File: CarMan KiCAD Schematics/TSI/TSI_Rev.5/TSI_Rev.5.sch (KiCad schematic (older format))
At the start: 26 parts, among them J1 J1, J10 J10, J11 J11, J12 J12, J13.1 Conn_01x06, J13.2 Conn_01x06, J14 J14, J15 J15, J16 J16, J17 J17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

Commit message: TSI Footprinting (100%) - Created symbol for connector J1
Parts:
- J1: footprint (none) -> TSI_Rev_2021_Footprint_Lib:Molex-0010844030; Note (none) -> This is custom, could not find on internet
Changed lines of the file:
@@
 F 0 "J1" H 900 950 50  0000 L CNN
 F 1 "J1" H 900 950 50  0001 L CNN
-F 2 "" H 950 750 50  0001 C CNN
+F 2 "TSI_Rev_2021_Footprint_Lib:Molex-0010844030" H 950 750 50  0001 C CNN
 F 3 "https://www.molex.com/pdm_docs/sd/010844020_sd.pdf" H 950 750 50  0001 C CNN
+F 4 "This is custom, could not find on internet" H 950 750 50  0001 C CNN "Note"
 	1    950  750
 	1    0    0    -1

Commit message: Started TSI PCB
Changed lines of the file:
@@
 F1 "PCDC_Circuit.sch" 79
 F2 "Throttle_HV" I R 3100 6400 50
-F3 "MC+" I L 1550 6000 50
+F3 "MC_Voltage" I L 1550 6000 50
 F4 "HV-" I L 1550 5900 50
 F5 "HV+" I L 1550 5800 50
-F6 "TSV_V" I L 1550 6100 50
+F6 "TSV_Voltage" I L 1550 6100 50
 F7 "IO_Ground" I R 3100 6500 50
 F8 "1.24VREF" I R 3100 6200 50
@@
 Brake_Pressed_HV
 Text Label 700  6000 0    50   ~ 0
-MC+
+MC_Voltage
 Wire Wire Line
 	1550 2800 2050 2800
@@
 	6200 6650 6800 6650
 $Sheet
-S 4800 6200 1400 1350
+S 4800 6200 1400 1400
 U 5F98EBE9
 F0 "Sensors_Throttle_Voltage" 50
@@
 F10 "Throttle_HV" I L 4800 7200 50
 F11 "TSV_Voltage" I L 4800 6900 50
-F12 "MC_Voltage" I L 4800 6800 50
+F12 "MC+" I L 4800 6800 50
 F13 "HV+" I L 4800 7000 50
 F14 "HV-" I L 4800 7100 50
 F15 "A1_HV" I L 4800 7300 50
 F16 "A2_HV" I L 4800 7400 50
+F17 "MC_Voltage" I L 4800 7500 50
 $EndSheet
 Text Notes 5650 6350 0    47   ~ 0
@@
 Text Notes 9650 3950 2    50   ~ 0
 LV\n
+Text Label 4200 7500 0    50   ~ 0
+MC_Voltage
+Wire Wire Line
+	4200 7500 4800 7500
 $EndSCHEMATC

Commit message: - Updated logic header footprints on TSI
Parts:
- J13.1, J13.2: footprint TSI_Rev_2021_Footprint_Lib:Molex_MiniFit-JR-5556-06A_2x03x4.20mm_Straight -> Connector_PinSocket_2.54mm:PinSocket_1x06_P2.54mm_Vertical
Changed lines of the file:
@@
 F 0 "J13.2" H 5950 2100 50  0000 L CNN
 F 1 "Conn_01x06" H 6180 1701 50  0001 L CNN
-F 2 "TSI_Rev_2021_Footprint_Lib:Molex_MiniFit-JR-5556-06A_2x03x4.20mm_Straight" H 6100 1800 50  0001 C CNN
+F 2 "Connector_PinSocket_2.54mm:PinSocket_1x06_P2.54mm_Vertical" H 6100 1800 50  0001 C CNN
 F 3 "~" H 6100 1800 50  0001 C CNN
 	1    6100 1800
@@
 F 0 "J13.1" H 5700 2100 50  0000 L CNN
 F 1 "Conn_01x06" H 5930 1701 50  0001 L CNN
-F 2 "TSI_Rev_2021_Footprint_Lib:Molex_MiniFit-JR-5556-06A_2x03x4.20mm_Straight" H 5850 1800 50  0001 C CNN
+F 2 "Connector_PinSocket_2.54mm:PinSocket_1x06_P2.54mm_Vertical" H 5850 1800 50  0001 C CNN
 F 3 "~" H 5850 1800 50  0001 C CNN
 	1    5850 1800

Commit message: Started TSI layout
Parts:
- J1: symbol Connector_Generic:Conn_01x04 -> Connector_Generic:Conn_01x03
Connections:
- no-connect marks 10 -> 9
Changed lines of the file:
@@
 Text Label 700  7300 0    50   ~ 0
 AIRS+
-NoConn ~ 750  950
-$Comp
-L Connector_Generic:Conn_01x04 J1
+$Comp
+L Connector_Generic:Conn_01x03 J1
 U 1 1 5FC3F568
 P 950 750
@@
 Text Label 11100 3500 2    50   ~ 0
 Drive_BTN
-$Comp
-L TSI_Rev.5-rescue:Current_Sensor-CarMan_KiCAD_Library-TSI_Rev.5-rescue J?
-U 1 1 5FA558BE
-P 950 1300
-AR Path="/5F98EBE9/5FA558BE" Ref="J?"  Part="1"
-AR Path="/5FA558BE" Ref="J2"  Part="1"
-F 0 "J2" H 950 1300 50  0000 C CNN
-F 1 "Current_Sensor" H 950 500 50  0000 C CNN
-F 2 "TSI_Rev_2021_Footprint_Lib:Current Sensor" H 950 1300 50  0001 C CNN
-F 3 "" H 950 1300 50  0001 C CNN
-	1    950  1300
-	1    0    0    -1
-$EndComp
 NoConn ~ 1350 1950
 NoConn ~ 1350 1450
@@
 Wire Wire Line
 	4200 7500 4800 7500
+$Comp
+L TSI_Rev.5-rescue:Current_Sensor-CarMan_KiCAD_Library-TSI_Rev.5-rescue J?
+U 1 1 5FA558BE
+P 950 1300
+AR Path="/5F98EBE9/5FA558BE" Ref="J?"  Part="1"
+AR Path="/5FA558BE" Ref="J2"  Part="1"
+F 0 "J2" H 950 1300 50  0000 C CNN
+F 1 "Current_Sensor" H 950 500 50  0000 C CNN
+F 2 "TSI_Rev_2021_Footprint_Lib:Current Sensor" H 950 1300 50  0001 C CNN
+F 3 "" H 950 1300 50  0001 C CNN
+	1    950  1300
+	1    0    0    -1
+$EndComp
 $EndSCHEMATC

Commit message: Organizational Added jumper between chassis ground and can shield
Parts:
- added JP3: Jumper, Connector_PinHeader_2.54mm:PinHeader_1x02_P2.54mm_Vertical, symbol Device:Jumper
- J19: footprint TSI_Rev_2021_Footprint_Lib:Molex_MiniFit-JR-5556-06A_2x03x4.20mm_Straight -> Connector_PinSocket_2.54mm:PinSocket_1x08_P2.54mm_Vertical; symbol Connector_Generic:Conn_01x06 -> Connector_Generic:Conn_01x08
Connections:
- net CAN_Shield: now also JP3.1; no longer J6.4 (Pin_4)
- new net Chassis_GND: J6.4 (Pin_4), JP3.2
- no-connect marks 9 -> 11
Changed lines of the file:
@@
 Text Label 4950 2100 0    50   ~ 0
 Throttle_SEL
-Text Label 5150 3450 0    50   ~ 0
+Text Label 5150 3600 0    50   ~ 0
 Flowrate_5V
-Text Label 6700 3450 2    50   ~ 0
+Text Label 6700 3600 2    50   ~ 0
 5V
-Text Label 5150 3550 0    50   ~ 0
+Text Label 5150 3700 0    50   ~ 0
 Flowrate_RTN
-Text Label 6700 3550 2    50   ~ 0
+Text Label 6700 3700 2    50   ~ 0
 GLV_RTN
 Text Label 7300 800  2    50   ~ 0
@@
 Text Label 7450 850  0    50   ~ 0
 CAN_Shield
-Text Label 7450 950  0    50   ~ 0
-Chassis_GND
 Text Label 7450 750  0    50   ~ 0
 BP_CAN-
@@
 Wire Notes Line
 	6550 2600 6550 3100
-Text Label 6700 3650 2    50   ~ 0
+Text Label 6700 3800 2    50   ~ 0
 GLV_RTN
-Text Label 5150 3650 0    50   ~ 0
+Text Label 5150 3800 0    50   ~ 0
 FAULT_LED_RTN
 Wire Notes Line
@@
 Text Label 2000 2250 0    50   ~ 0
 Safety_Loop
-Text Label 6700 3350 2    49   ~ 0
+Text Label 6700 3500 2    49   ~ 0
 MRESET_Contact
-Text Label 5150 3350 0    49   ~ 0
+Text Label 5150 3500 0    49   ~ 0
 GEN_Fault_LED
 Text Label 4950 1800 0    49   ~ 0
@@
 Text Label 700  4950 0    50   ~ 0
 Flowrate
-Text Label 6700 3250 2    50   ~ 0
+Text Label 6700 3400 2    50   ~ 0
 Brake_Light
-Text Label 5150 3250 0    50   ~ 0
+Text Label 5150 3400 0    50   ~ 0
 Brake_Pressed
-Text Label 5150 3750 0    50   ~ 0
+Text Label 5150 3900 0    50   ~ 0
 Brake_Light_RTN
-Text Label 6700 3750 2    50   ~ 0
+Text Label 6700 3900 2    50   ~ 0
 GLV_RTN
 Text Label 11100 3600 2    50   ~ 0
@@
 Text Label 8100 5900 0    50   ~ 0
 COOL_24V
-Text Notes 7750 1250 0    50   ~ 0
-Battery Pack\nto TSI\n\n
 $Comp
 L Connector_Generic:Conn_01x04 J6
@@
 	5300 750  5600 750
 Wire Wire Line
-	5150 3250 6700 3250
-Wire Wire Line
-	5150 3350 6700 3350
-Wire Wire Line
-	5150 3450 6700 3450
-Wire Wire Line
-	5150 3550 6700 3550
-Wire Wire Line
-	5150 3650 6700 3650
-Wire Wire Line
-	5150 3750 6700 3750
-Wire Wire Line
-	5150 3850 6700 3850
-Text Label 5150 3850 0    50   ~ 0
+	5150 3400 6700 3400
+Wire Wire Line
+	5150 3500 6700 3500
+Wire Wire Line
+	5150 3600 6700 3600
+Wire Wire Line
+	5150 3700 6700 3700
+Wire Wire Line
+	5150 3800 6700 3800
+Wire Wire Line
+	5150 3900 6700 3900
+Wire Wire Line
+	5150 4000 6700 4000
+Text Label 5150 4000 0    50   ~ 0
 SCL_uC
-Text Label 6700 3850 2    50   ~ 0
+Text Label 6700 4000 2    50   ~ 0
 SCL_TSI
-Text Label 6200 3850 0    50   ~ 0
+Text Label 6200 4000 0    50   ~ 0
 SCL
 Wire Wire Line
-	5150 3950 6700 3950
-Text Label 5150 3950 0    50   ~ 0
+	5150 4100 6700 4100
+Text Label 5150 4100 0    50   ~ 0
 SDA_uC
-Text Label 6200 3950 0    50   ~ 0
+Text Label 6200 4100 0    50   ~ 0
 SDA
-Text Label 6700 3950 2    50   ~ 0
+Text Label 6700 4100 2    50   ~ 0
 SDA_TSI
 Text Label 700  6200 0    50   ~ 0
@@
 Text Label 1550 3100 0    50   ~ 0
 IMD_Status
-Text Notes 1600 3450 0    50   ~ 0
+Text Notes 1650 3650 0    50   ~ 0
 Testing Connector\n\n
 $Comp
-L Connector_Generic:Conn_01x06 J19
+L Connector_Generic:Conn_01x08 J19
 U 1 1 5FE0EFE1
-P 2250 2900
-F 0 "J19" H 2200 3200 50  0000 L CNN
-F 1 "J19" H 2200 3200 50  0001 L CNN
-F 2 "TSI_Rev_2021_Footprint_Lib:Molex_MiniFit-JR-5556-06A_2x03x4.20mm_Straight" H 2250 2900 50  0001 C CNN
-F 3 "~" H 2250 2900 50  0001 C CNN
-	1    2250 2900
+P 2250 3000
+F 0 "J19" H 2200 3400 50  0000 L CNN
+F 1 "J19" H 2200 3300 50  0001 L CNN
+F 2 "Connector_PinSocket_2.54mm:PinSocket_1x08_P2.54mm_Vertical" H 2250 3000 50  0001 C CNN
+F 3 "~" H 2250 3000 50  0001 C CNN
+	1    2250 3000
 	1    0    0    -1
 $EndComp
@@
 5V
 Wire Wire Line
-	5150 4050 6700 4050
-Text Label 5150 4050 0    50   ~ 0
+	5150 4200 6700 4200
+Text Label 5150 4200 0    50   ~ 0
 TSAL_RTN
-Text Label 6700 4050 2    50   ~ 0
+Text Label 6700 4200 2    50   ~ 0
 GLV_RTN
 $Comp
@@
 $EndComp
 Wire Wire Line
-	5150 4150 6700 4150
-Text Label 5150 4150 0    50   ~ 0
+	5150 4300 6700 4300
+Text Label 5150 4300 0    50   ~ 0
 AIRS-
-Text Label 6700 4150 2    50   ~ 0
+Text Label 6700 4300 2    50   ~ 0
 GLV_RTN
 $Comp
@@
 Wire Wire Line
 	5950 4850 6450 4850
-Wire Wire Line
-	7450 850  7450 950
-Connection ~ 7450 950
 $Comp
 L power:PWR_FLAG #FLG0101
@@
 Text Label 10400 750  0    49   ~ 0
 GLV_RTN
-Text Label 10400 850  0    50   ~ 0
-SL1_In
 $Sheet
 S 8850 2950 1500 1450
@@
 	1    0    0    -1
 $EndComp
+NoConn ~ 2050 3300
+NoConn ~ 2050 3400
+$Comp
+L Device:Jumper JP?
+U 1 1 601967AD
+P 5900 3300
+AR Path="/6196BF15/601967AD" Ref="JP?"  Part="1"
+AR Path="/601967AD" Ref="JP3"  Part="1"
+F 0 "JP3" H 6100 3400 50  0000 R CNN
+F 1 "Jumper" H 6600 3300 50  0001 R CNN
+F 2 "Connector_PinHeader_2.54mm:PinHeader_1x02_P2.54mm_Vertical" H 5900 3300 50  0001 C CNN
+F 3 "~" H 5900 3300 50  0001 C CNN
+	1    5900 3300
+	1    0    0    -1
+$EndComp
+Text Label 5150 3300 0    50   ~ 0
+CAN_Shield
+Text Label 6700 3300 2    50   ~ 0
+Chassis_GND
+Wire Wire Line
+	6700 3300 6200 3300
+Wire Wire Line
+	5150 3300 5600 3300
+Text Notes 7550 1250 0    50   ~ 0
+Battery Pack\nto TSI\n\n
+Text Label 7450 950  0    50   ~ 0
+Chassis_GND
+Text Label 10400 850  0    50   ~ 0
+SL1_In
 $EndSCHEMATC

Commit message: TSI (~97%)
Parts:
- added J21: J21, Connector_PinSocket_2.54mm:PinSocket_1x04_P2.54mm_Vertical, symbol Connector_Generic:Conn_01x04
- added J23: J23, Connector_PinSocket_2.54mm:PinSocket_1x02_P2.54mm_Vertical, symbol Connector_Generic:Conn_01x02
- J19: footprint Connector_PinSocket_2.54mm:PinSocket_1x08_P2.54mm_Vertical -> Connector_PinSocket_2.54mm:PinSocket_1x04_P2.54mm_Vertical; symbol Connector_Generic:Conn_01x08 -> Connector_Generic:Conn_01x04
- J22: renamed from J21; value J21 -> J22
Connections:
- net IMD_Status: now also J19.3 (Pin_3); no longer J19.5 (Pin_5)
- net PC_Ready: now also J19.1 (Pin_1); no longer J19.3 (Pin_3)
- net SCL: now also J23.2 (Pin_2); no longer J19.2 (Pin_2)
- net SDA: now also J23.1 (Pin_1); no longer J19.1 (Pin_1)
- net SL1_In: now also J19.2 (Pin_2); no longer J19.4 (Pin_4)
- net Throttle_SEL: now also J19.4 (Pin_4); no longer J19.6 (Pin_6)
- no-connect marks 11 -> 13
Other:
- note added: "Left Side\nTesting Connector\n\n"
- note added: "Right Side\nTesting Connector\n\n"
- note removed: "Testing Connector\n\n"
- moved on the sheet: J22
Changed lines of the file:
@@
 Text Label 2000 1750 0    50   ~ 0
 AMS_FAULT_LED
+Text Label 4400 2800 0    50   ~ 0
+SCL
 Text Label 1550 2800 0    50   ~ 0
-SCL
-Text Label 1550 3000 0    50   ~ 0
 SL1_In
-Text Label 1550 2700 0    50   ~ 0
+Text Label 4400 2700 0    50   ~ 0
 SDA
 Text Label 550  2700 0    50   ~ 0
@@
 	10400 950  10850 950
 Wire Wire Line
-	1550 2700 2050 2700
-Wire Wire Line
 	2000 1750 2600 1750
 Text Label 11100 4800 2    50   ~ 0
@@
 Text Label 11100 6100 2    50   ~ 0
 IMD_FAULT_LED
-Text Notes 2550 3250 0    50   ~ 0
+Text Notes 3300 3250 0    50   ~ 0
 LSP IMD & AMS Reset \nButton\n
-Text Label 2550 2700 0    50   ~ 0
+Text Label 3300 2700 0    50   ~ 0
 IMD_Status
-Text Label 2550 2800 0    50   ~ 0
+Text Label 3300 2800 0    50   ~ 0
 IMD_Button_RTN
 Wire Wire Line
-	2550 2800 3200 2800
-Wire Wire Line
-	2550 2700 3200 2700
+	3300 2800 3950 2800
+Wire Wire Line
+	3300 2700 3950 2700
 Text Label 11100 6000 2    50   ~ 0
 IMD_Button_RTN
@@
 MC_Voltage
 Wire Wire Line
+	1550 2700 2050 2700
+Wire Wire Line
+	1550 3000 2050 3000
+Wire Wire Line
+	1550 2900 2050 2900
+Wire Wire Line
 	1550 2800 2050 2800
-Wire Wire Line
-	1550 2900 2050 2900
-Wire Wire Line
-	1550 3200 2050 3200
-Wire Wire Line
-	1550 3100 2050 3100
-Wire Wire Line
-	1550 3000 2050 3000
+Text Label 1550 2700 0    50   ~ 0
+PC_Ready
+Text Label 1550 3000 0    50   ~ 0
+Throttle_SEL
 Text Label 1550 2900 0    50   ~ 0
-PC_Ready
-Text Label 1550 3200 0    50   ~ 0
-Throttle_SEL
-Text Label 1550 3100 0    50   ~ 0
 IMD_Status
-Text Notes 1650 3650 0    50   ~ 0
-Testing Connector\n\n
-$Comp
-L Connector_Generic:Conn_01x08 J19
+Text Notes 1600 3250 0    50   ~ 0
+Left Side\nTesting Connector\n\n
+$Comp
+L Connector_Generic:Conn_01x04 J19
 U 1 1 5FE0EFE1
-P 2250 3000
-F 0 "J19" H 2200 3400 50  0000 L CNN
-F 1 "J19" H 2200 3300 50  0001 L CNN
-F 2 "Connector_PinSocket_2.54mm:PinSocket_1x08_P2.54mm_Vertical" H 2250 3000 50  0001 C CNN
-F 3 "~" H 2250 3000 50  0001 C CNN
-	1    2250 3000
+P 2250 2800
+F 0 "J19" H 2200 3000 50  0000 L CNN
+F 1 "J19" H 2200 3100 50  0001 L CNN
+F 2 "Connector_PinSocket_2.54mm:PinSocket_1x04_P2.54mm_Vertical" H 2250 2800 50  0001 C CNN
+F 3 "~" H 2250 2800 50  0001 C CNN
+	1    2250 2800
 	1    0    0    -1
 $EndComp
@@
 $EndComp
 $Comp
-L Connector_Generic:Conn_01x04 J21
+L Connector_Generic:Conn_01x04 J22
 U 1 1 5FDCB93A
-P 3400 2800
-F 0 "J21" H 3350 3000 50  0000 L CNN
-F 1 "J21" H 3350 3000 50  0001 L CNN
-F 2 "TSI_Rev_2021_Footprint_Lib:Molex_MiniFit-JR-5556-04A_2x02x4.20mm_Straight" H 3400 2800 50  0001 C CNN
-F 3 "~" H 3400 2800 50  0001 C CNN
-	1    3400 2800
-	1    0    0    -1
-$EndComp
-Text Label 2550 2900 0    50   ~ 0
+P 4150 2800
+F 0 "J22" H 4100 3000 50  0000 L CNN
+F 1 "J22" H 4100 3000 50  0001 L CNN
+F 2 "TSI_Rev_2021_Footprint_Lib:Molex_MiniFit-JR-5556-04A_2x02x4.20mm_Straight" H 4150 2800 50  0001 C CNN
+F 3 "~" H 4150 2800 50  0001 C CNN
+	1    4150 2800
+	1    0    0    -1
+$EndComp
+Text Label 3300 2900 0    50   ~ 0
 AMS_Status
-Text Label 2550 3000 0    50   ~ 0
+Text Label 3300 3000 0    50   ~ 0
 AMS_Button_RTN
 Wire Wire Line
-	2550 3000 3200 3000
-Wire Wire Line
-	2550 2900 3200 2900
+	3300 3000 3950 3000
+Wire Wire Line
+	3300 2900 3950 2900
 Wire Wire Line
 	3600 950  2950 950
@@
 	1    0    0    -1
 $EndComp
-NoConn ~ 2050 3300
-NoConn ~ 2050 3400
 $Comp
 L Device:Jumper JP?
@@
 Text Label 10400 850  0    50   ~ 0
 SL1_In
+$Comp
+L Connector_Generic:Conn_01x02 J23
+U 1 1 600AD19A
+P 4800 2700
+F 0 "J23" H 4750 2800 50  0000 L CNN
+F 1 "J23" H 4750 2800 50  0001 L CNN
+F 2 "Connector_PinSocket_2.54mm:PinSocket_1x02_P2.54mm_Vertical" H 4800 2700 50  0001 C CNN
+F 3 "~" H 4800 2700 50  0001 C CNN
+	1    4800 2700
+	1    0    0    -1
+$EndComp
+Wire Wire Line
+	4600 2800 4400 2800
+Wire Wire Line
+	4600 2700 4400 2700
+Text Notes 2450 3250 0    50   ~ 0
+Right Side\nTesting Connector\n\n
+NoConn ~ 2800 2700
+NoConn ~ 2800 2800
+NoConn ~ 2800 2900
+$Comp
+L Connector_Generic:Conn_01x04 J21
+U 1 1 60224CCE
+P 3000 2800
+F 0 "J21" H 2950 3000 50  0000 L CNN
+F 1 "J21" H 2950 3100 50  0001 L CNN
+F 2 "Connector_PinSocket_2.54mm:PinSocket_1x04_P2.54mm_Vertical" H 3000 2800 50  0001 C CNN
+F 3 "~" H 3000 2800 50  0001 C CNN
+	1    3000 2800
+	1    0    0    -1
+$EndComp
+NoConn ~ 2800 3000
 $EndSCHEMATC

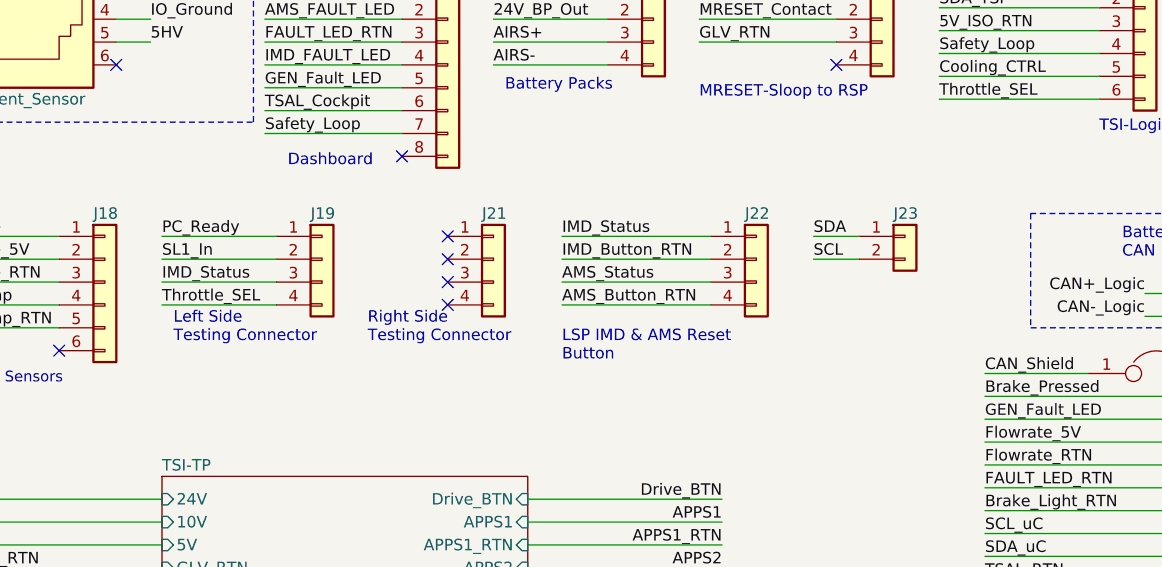
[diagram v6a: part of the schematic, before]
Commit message: TSI (~98%) - Added right side testing connector - Finish left side testing connector - Added Caps to HV side
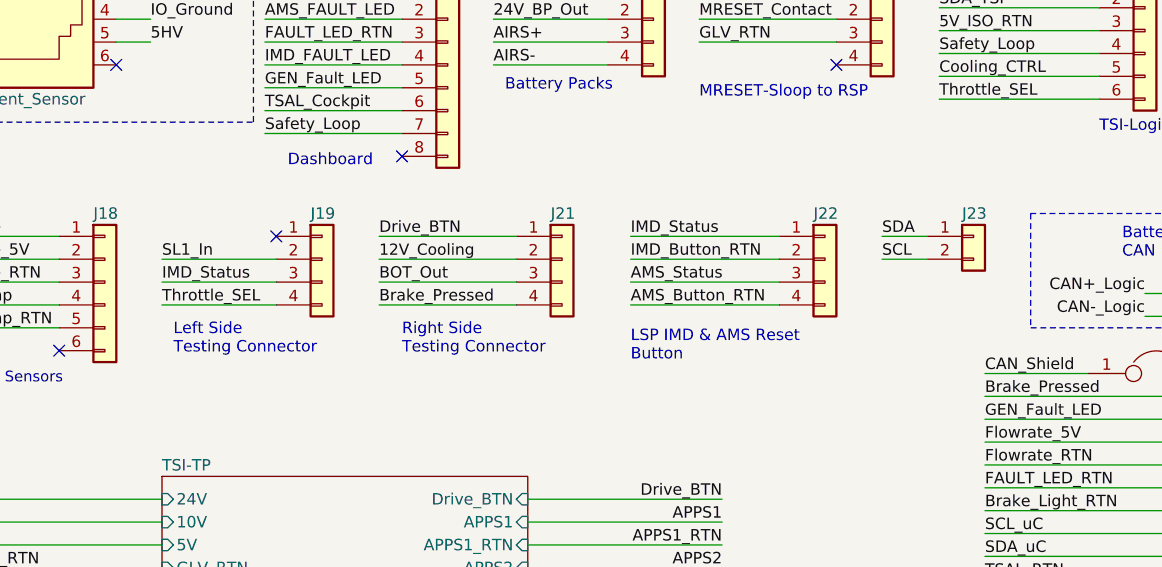
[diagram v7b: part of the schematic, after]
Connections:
- net 12V_Cooling: now also J21.2 (Pin_2)
- net BOT_Out: now also J21.3 (Pin_3)
- net Brake_Light: now also J21.4 (Pin_4)
- net Drive_BTN: now also J21.1 (Pin_1)
- net PC_Ready: no longer J19.1 (Pin_1)
- no-connect marks 13 -> 10
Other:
- moved on the sheet: J21, J22, J23
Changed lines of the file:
@@
 Text Label 2000 1750 0    50   ~ 0
 AMS_FAULT_LED
-Text Label 4400 2800 0    50   ~ 0
+Text Label 4700 2800 0    50   ~ 0
 SCL
 Text Label 1550 2800 0    50   ~ 0
 SL1_In
-Text Label 4400 2700 0    50   ~ 0
+Text Label 4700 2700 0    50   ~ 0
 SDA
 Text Label 550  2700 0    50   ~ 0
@@
 Text Label 6700 3400 2    50   ~ 0
 Brake_Light
-Text Label 5150 3400 0    50   ~ 0
-Brake_Pressed
 Text Label 5150 3900 0    50   ~ 0
 Brake_Light_RTN
@@
 Text Label 11100 6100 2    50   ~ 0
 IMD_FAULT_LED
-Text Notes 3300 3250 0    50   ~ 0
+Text Notes 3600 3250 0    50   ~ 0
 LSP IMD & AMS Reset \nButton\n
-Text Label 3300 2700 0    50   ~ 0
+Text Label 3600 2700 0    50   ~ 0
 IMD_Status
-Text Label 3300 2800 0    50   ~ 0
+Text Label 3600 2800 0    50   ~ 0
 IMD_Button_RTN
 Wire Wire Line
-	3300 2800 3950 2800
-Wire Wire Line
-	3300 2700 3950 2700
+	3600 2800 4250 2800
+Wire Wire Line
+	3600 2700 4250 2700
 Text Label 11100 6000 2    50   ~ 0
 IMD_Button_RTN
@@
 MC_Voltage
 Wire Wire Line
-	1550 2700 2050 2700
-Wire Wire Line
 	1550 3000 2050 3000
 Wire Wire Line
@@
 Wire Wire Line
 	1550 2800 2050 2800
-Text Label 1550 2700 0    50   ~ 0
-PC_Ready
 Text Label 1550 3000 0    50   ~ 0
 Throttle_SEL
 Text Label 1550 2900 0    50   ~ 0
 IMD_Status
-Text Notes 1600 3250 0    50   ~ 0
+Text Notes 1600 3300 0    50   ~ 0
 Left Side\nTesting Connector\n\n
 $Comp
@@
 L Connector_Generic:Conn_01x04 J22
 U 1 1 5FDCB93A
-P 4150 2800
-F 0 "J22" H 4100 3000 50  0000 L CNN
-F 1 "J22" H 4100 3000 50  0001 L CNN
-F 2 "TSI_Rev_2021_Footprint_Lib:Molex_MiniFit-JR-5556-04A_2x02x4.20mm_Straight" H 4150 2800 50  0001 C CNN
-F 3 "~" H 4150 2800 50  0001 C CNN
-	1    4150 2800
-	1    0    0    -1
-$EndComp
-Text Label 3300 2900 0    50   ~ 0
+P 4450 2800
+F 0 "J22" H 4400 3000 50  0000 L CNN
+F 1 "J22" H 4400 3000 50  0001 L CNN
+F 2 "TSI_Rev_2021_Footprint_Lib:Molex_MiniFit-JR-5556-04A_2x02x4.20mm_Straight" H 4450 2800 50  0001 C CNN
+F 3 "~" H 4450 2800 50  0001 C CNN
+	1    4450 2800
+	1    0    0    -1
+$EndComp
+Text Label 3600 2900 0    50   ~ 0
 AMS_Status
-Text Label 3300 3000 0    50   ~ 0
+Text Label 3600 3000 0    50   ~ 0
 AMS_Button_RTN
 Wire Wire Line
-	3300 3000 3950 3000
-Wire Wire Line
-	3300 2900 3950 2900
+	3600 3000 4250 3000
+Wire Wire Line
+	3600 2900 4250 2900
 Wire Wire Line
 	3600 950  2950 950
@@
 L Connector_Generic:Conn_01x02 J23
 U 1 1 600AD19A
-P 4800 2700
-F 0 "J23" H 4750 2800 50  0000 L CNN
-F 1 "J23" H 4750 2800 50  0001 L CNN
-F 2 "Connector_PinSocket_2.54mm:PinSocket_1x02_P2.54mm_Vertical" H 4800 2700 50  0001 C CNN
-F 3 "~" H 4800 2700 50  0001 C CNN
-	1    4800 2700
-	1    0    0    -1
-$EndComp
-Wire Wire Line
-	4600 2800 4400 2800
-Wire Wire Line
-	4600 2700 4400 2700
-Text Notes 2450 3250 0    50   ~ 0
+P 5100 2700
+F 0 "J23" H 5050 2800 50  0000 L CNN
+F 1 "J23" H 5050 2800 50  0001 L CNN
+F 2 "Connector_PinSocket_2.54mm:PinSocket_1x02_P2.54mm_Vertical" H 5100 2700 50  0001 C CNN
+F 3 "~" H 5100 2700 50  0001 C CNN
+	1    5100 2700
+	1    0    0    -1
+$EndComp
+Wire Wire Line
+	4900 2800 4700 2800
+Wire Wire Line
+	4900 2700 4700 2700
+Text Notes 2600 3300 0    50   ~ 0
 Right Side\nTesting Connector\n\n
-NoConn ~ 2800 2700
-NoConn ~ 2800 2800
-NoConn ~ 2800 2900
 $Comp
 L Connector_Generic:Conn_01x04 J21
 U 1 1 60224CCE
-P 3000 2800
-F 0 "J21" H 2950 3000 50  0000 L CNN
-F 1 "J21" H 2950 3100 50  0001 L CNN
-F 2 "Connector_PinSocket_2.54mm:PinSocket_1x04_P2.54mm_Vertical" H 3000 2800 50  0001 C CNN
-F 3 "~" H 3000 2800 50  0001 C CNN
-	1    3000 2800
-	1    0    0    -1
-$EndComp
-NoConn ~ 2800 3000
+P 3300 2800
+F 0 "J21" H 3250 3000 50  0000 L CNN
+F 1 "J21" H 3250 3100 50  0001 L CNN
+F 2 "Connector_PinSocket_2.54mm:PinSocket_1x04_P2.54mm_Vertical" H 3300 2800 50  0001 C CNN
+F 3 "~" H 3300 2800 50  0001 C CNN
+	1    3300 2800
+	1    0    0    -1
+$EndComp
+Text Label 5150 3400 0    50   ~ 0
+Brake_Pressed
+Text Label 2500 3000 0    50   ~ 0
+Brake_Pressed
+Text Label 2500 2900 0    50   ~ 0
+BOT_Out
+Text Label 2500 2800 0    49   ~ 0
+12V_Cooling
+Text Label 2500 2700 0    50   ~ 0
+Drive_BTN
+Wire Wire Line
+	2500 2700 3100 2700
+Wire Wire Line
+	3100 2800 2500 2800
+Wire Wire Line
+	2500 2900 3100 2900
+Wire Wire Line
+	3100 3000 2500 3000
+NoConn ~ 2050 2700
 $EndSCHEMATC
